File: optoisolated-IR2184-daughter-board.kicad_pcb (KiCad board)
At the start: 2 copper layers, 3 parts, among them J1 Conn_01x08_Pin, U1 IR2184, U2 6N137

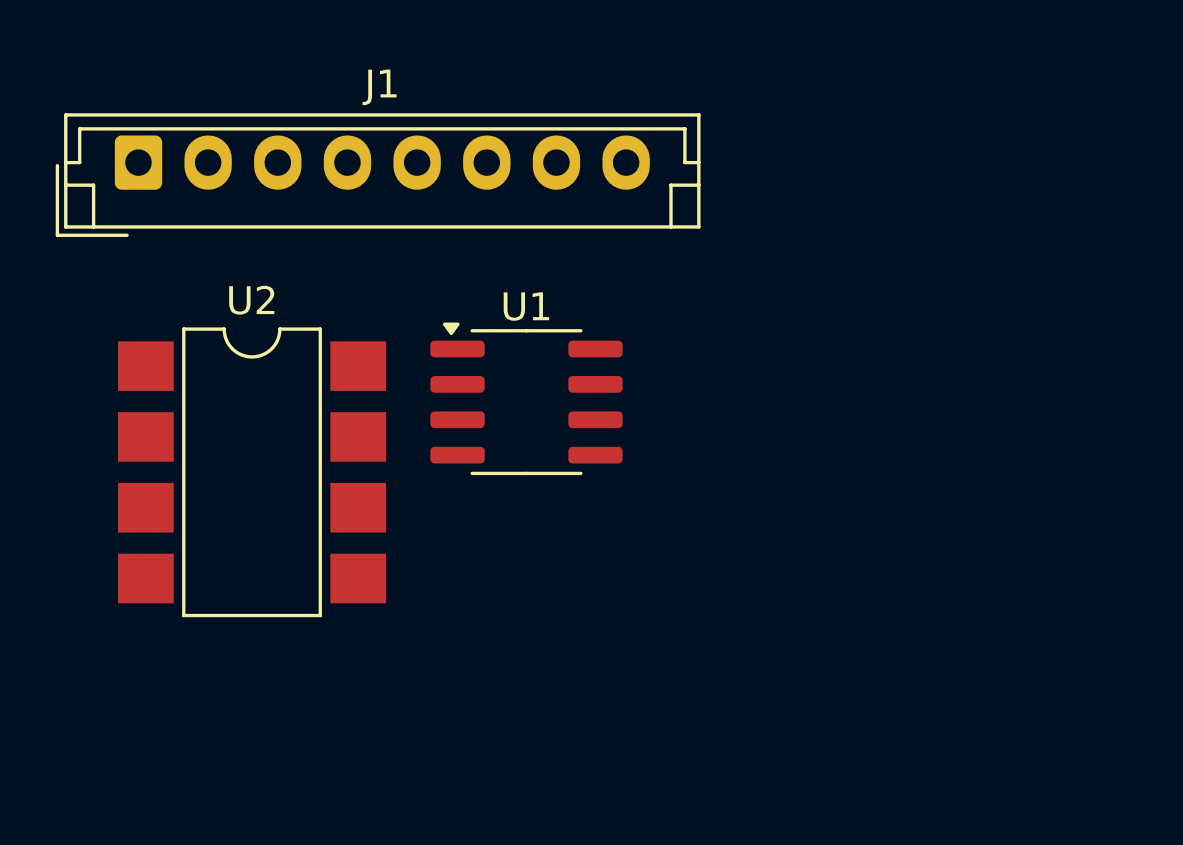
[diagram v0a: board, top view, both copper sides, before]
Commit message: placed most parts
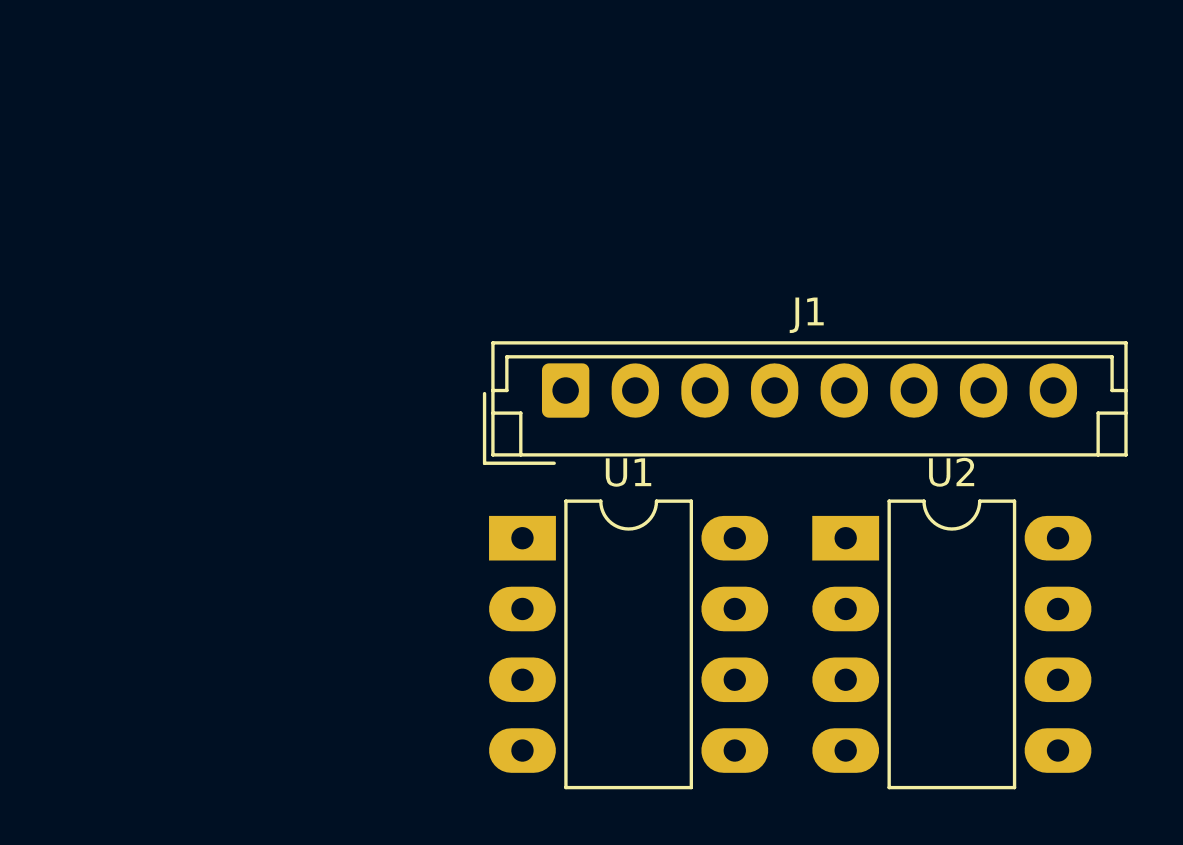
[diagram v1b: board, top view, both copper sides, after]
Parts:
- U1: footprint Package_SO:SOIC-8_3.9x4.9mm_P1.27mm -> Package_DIP:DIP-8_W7.62mm_LongPads
- U2: footprint Package_DIP:SMDIP-8_W7.62mm -> Package_DIP:DIP-8_W7.62mm_LongPads
- moved U2 21.4 mm to (153.8, 89.0)
- moved J1 17.4 mm to (143.7, 83.7)
- moved U1 4.89 mm to (142.2, 89.0)
